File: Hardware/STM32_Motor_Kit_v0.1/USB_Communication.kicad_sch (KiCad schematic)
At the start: 7 parts, among them J8 USB_B_Mini, U17 TVS_Diode_USB

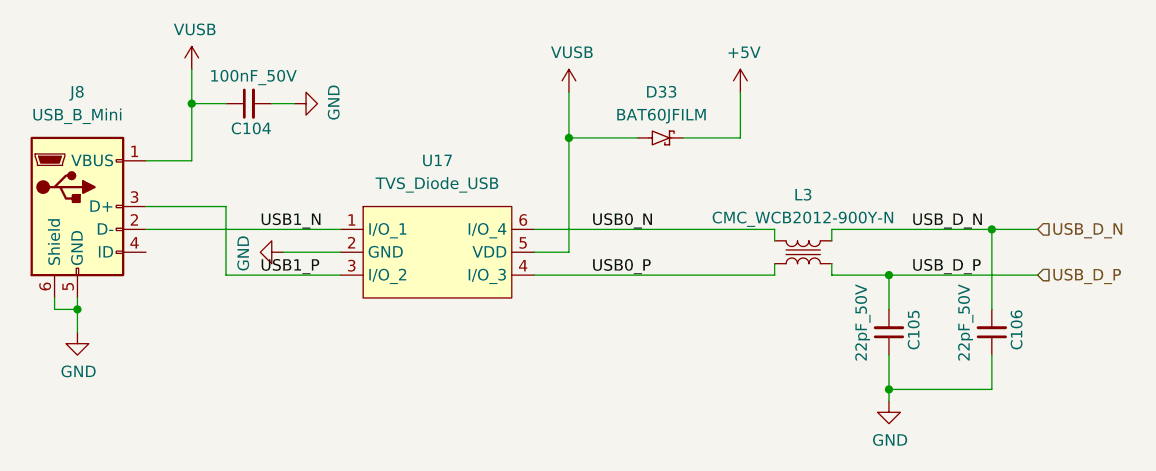
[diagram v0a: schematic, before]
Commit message: Şemada güncellemeler yaptım, PCB'de revizyon yapılacak
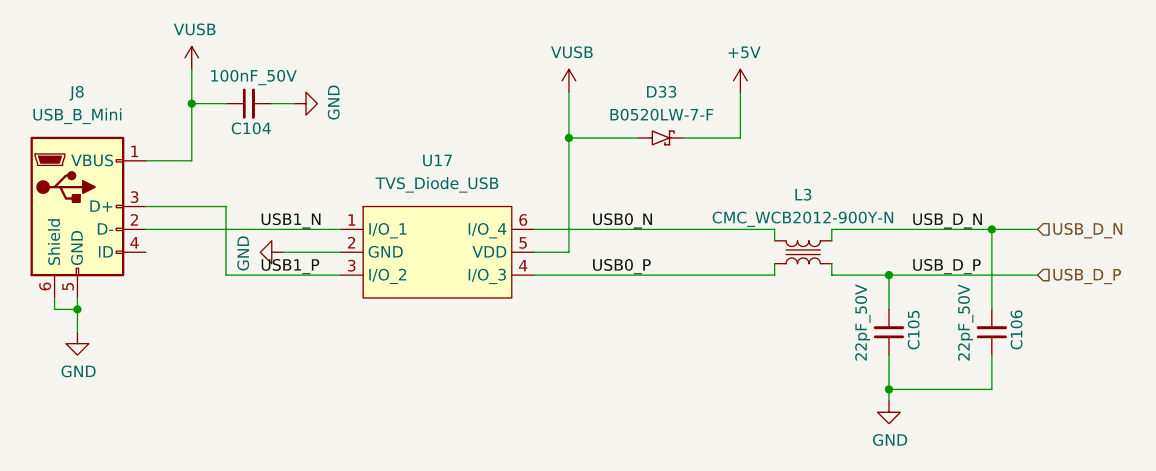
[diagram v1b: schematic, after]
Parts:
- D33: value BAT60JFILM -> B0520LW-7-F
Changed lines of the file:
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@@
 			)
 		)
-		(property "Value" "BAT60JFILM"
+		(property "Value" "B0520LW-7-F"
 			(at 120.777 69.85 0)
 			(effects
@@
 			)
 		)
-		(property "Description" "DIODE SCHOTTKY 3A 10V SOD323 ST "
+		(property "Description" "DIODE SCHOTTKY 3A 10V SOD323 ST"
 			(at 123.19 71.12 0)
 			(effects
@@
 			)
 		)
-		(property "Description" "DIODE TVS 5V 17.5V SOT23-6 "
+		(property "Description" "DIODE TVS 5V 17.5V SOT23-6"
 			(at 94.996 94.742 0)
 			(effects
@@
 			)
 		)
-		(property "Description" "CHOKE COMMON MODE 90R 400MA SMT "
+		(property "Description" "CHOKE COMMON MODE 90R 400MA SMT"
 			(at 138.43 92.71 0)
 			(effects

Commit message: 12.01.2025
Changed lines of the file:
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@@
 			(effects
 				(font
-					(size 1.27 1.27)
+					(face "Arial")
+					(size 0.635 0.635)
 				)
 			)
@@
 			(effects
 				(font
-					(size 1.27 1.27)
+					(face "Arial")
+					(size 0.635 0.635)
 				)
 				(hide yes)
@@
 			(effects
 				(font
-					(size 1.27 1.27)
+					(face "Arial")
+					(size 0.635 0.635)
 				)
 			)
@@
 			(effects
 				(font
-					(size 1.27 1.27)
+					(face "Arial")
+					(size 0.635 0.635)
 				)
 				(hide yes)
@@
 			(effects
 				(font
-					(size 1.27 1.27)
+					(face "Arial")
+					(size 0.635 0.635)
 				)
 				(hide yes)
@@
 			(effects
 				(font
-					(size 1.27 1.27)
+					(face "Arial")
+					(size 0.635 0.635)
 				)
 			)
@@
 			(effects
 				(font
-					(size 1.27 1.27)
+					(face "Arial")
+					(size 0.635 0.635)
 				)
 				(hide yes)
@@
 			(effects
 				(font
-					(size 1.27 1.27)
+					(face "Arial")
+					(size 0.635 0.635)
 				)
 				(hide yes)
@@
 			(effects
 				(font
-					(size 1.27 1.27)
+					(face "Arial")
+					(size 0.635 0.635)
 				)
 				(justify left)
@@
 			(effects
 				(font
-					(size 1.27 1.27)
+					(face "Arial")
+					(size 0.635 0.635)
 				)
 			)
@@
 			(effects
 				(font
-					(size 1.27 1.27)
+					(face "Arial")
+					(size 0.635 0.635)
 				)
 				(justify left)
@@
 			(effects
 				(font
-					(size 1.27 1.27)
+					(face "Arial")
+					(size 0.635 0.635)
 				)
 				(justify left)
@@
 			(effects
 				(font
-					(size 1.27 1.27)
+					(face "Arial")
+					(size 0.635 0.635)
 				)
 				(hide yes)
@@
 			(effects
 				(font
-					(size 1.27 1.27)
-				)
-				(hide yes)
+					(face "Arial")
+					(size 0.635 0.635)
+				)
+				(hide yes)

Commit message: Şema üzerinde değişiklikler devam ediyor
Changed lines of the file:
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@@
 (kicad_sch
-	(version 20231120)
+	(version 20250114)
 	(generator "eeschema")
-	(generator_version "8.0")
+	(generator_version "9.0")
 	(paper "A4")
 	(junction
@@
 	(label "USB1_N"
 		(at 76.2 82.55 0)
-		(fields_autoplaced yes)
 		(effects
 			(font
@@
 	(label "USB0_P"
 		(at 113.03 87.63 0)
-		(fields_autoplaced yes)
 		(effects
 			(font
@@
 	(label "USB0_N"
 		(at 113.03 82.55 0)
-		(fields_autoplaced yes)
 		(effects
 			(font
@@
 	(label "USB_D_N"
 		(at 148.59 82.55 0)
-		(fields_autoplaced yes)
 		(effects
 			(font
@@
 	(label "USB1_P"
 		(at 76.2 87.63 0)
-		(fields_autoplaced yes)
 		(effects
 			(font
@@
 	(label "USB_D_P"
 		(at 148.59 87.63 0)
-		(fields_autoplaced yes)
 		(effects
 			(font
@@
 		(shape input)
 		(at 162.56 87.63 0)
-		(fields_autoplaced yes)
 		(effects
 			(font
@@
 		(shape input)
 		(at 162.56 82.55 0)
-		(fields_autoplaced yes)
-		(effects
-			(font
+		(effects
+			(font
